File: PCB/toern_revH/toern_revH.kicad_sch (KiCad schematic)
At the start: 123 parts, among them IC1 BQ24075TRGTR, J1 AudioJack3_Switch, J10 Conn_01x02, J11 Conn_01x05, J11.5 Conn_01x05, J12 Conn_01x05, J13 Conn_01x05, J14 Conn_01x05, J15 Conn_01x05, J16 Conn_01x02, J17 AudioJack3_Ground, J18 Conn_01x05_Socket, J19 Conn_01x05_Socket, J2 Conn_01x05_Socket, J20 Conn_01x05_Socket, J21 Conn_01x05_Socket, J22 Conn_01x05_Socket, J23 Conn_01x05_Socket, J24 Conn_01x05_Socket, J25 Conn_01x02, J26 Conn_01x02, J3 AudioJack3_Ground, J4 USB_C_Receptacle_USB2.0, J5 AudioJack3_Switch, J6 AudioJack3_Switch, J7 AudioJack3_Switch, J8 Micro_SD_Card, J9 Conn_01x03, U1 SPX3819M5-L-3-3, U10 01x05 Connector_PinSocket_2.5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, U11 01x05 Connector_PinSocket_2.5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, U12 01x05 Connector_PinSocket_2.5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, U13 PAM8403D, U14 74LVC1G17, U15 74AHCT1G125, U2 SPX3819M5-L-1-8, U3 SGTL5000XNBA3, U4 TLP2361V4_E, U5 74LVC2G14, U6 Teensy4.1, U7 SPX3819M5-L-3-3, U8 TPS22918DBVR, U9 01x05 Connector_PinSocket_2.5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

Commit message: fixed production files for revH
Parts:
- removed TP1, TP2: TestPoint, symbol Connector:TestPoint
- C32: value 10uF -> 10u
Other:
- moved on the sheet: C21, C22, C38, J26, J8, R16, R29, R30, U14

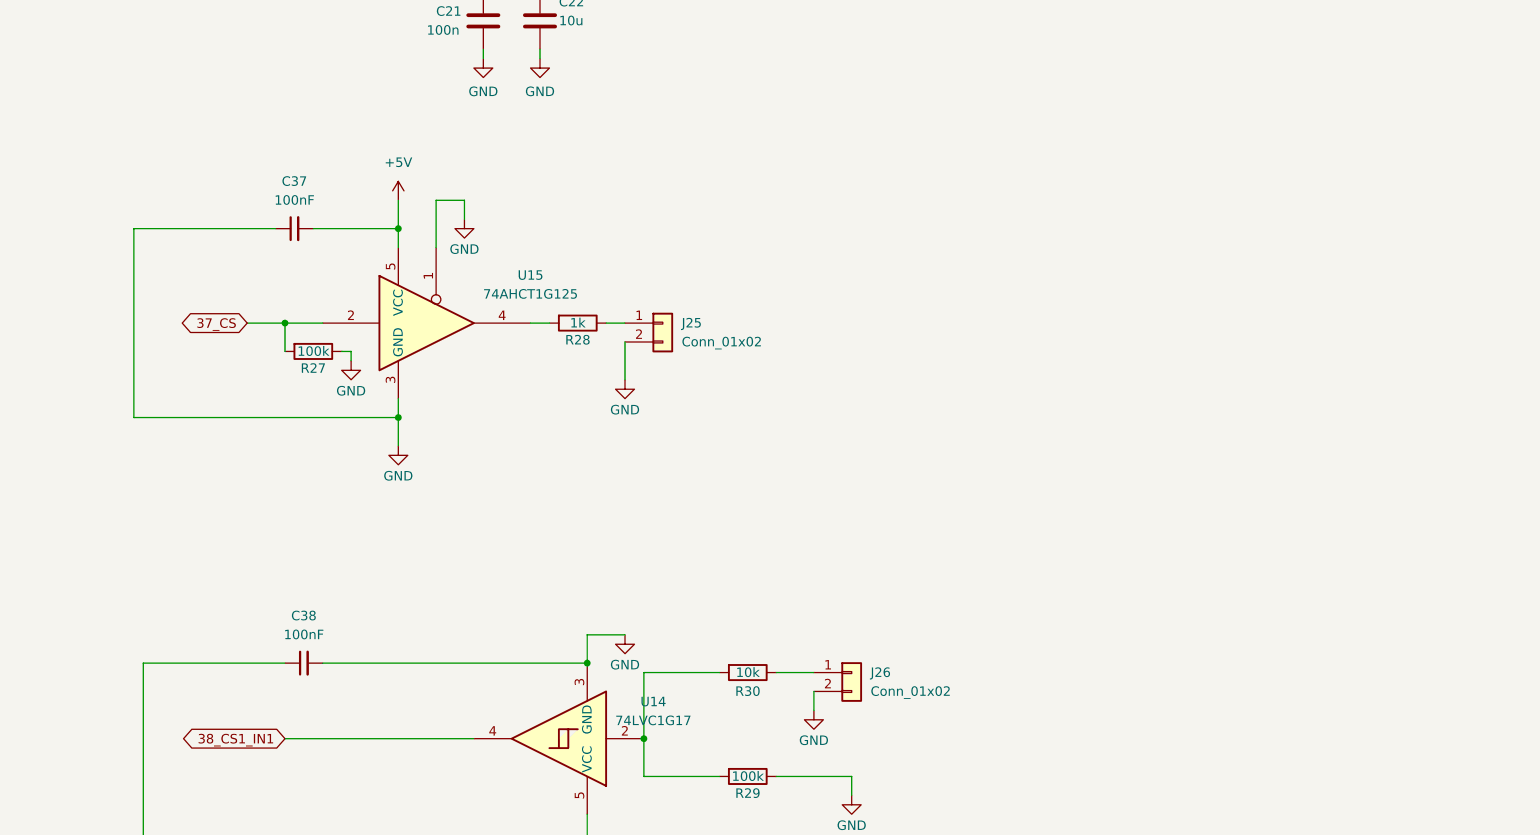
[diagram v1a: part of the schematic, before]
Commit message: added protection for 5-12v clock input as well as 2nd clockout
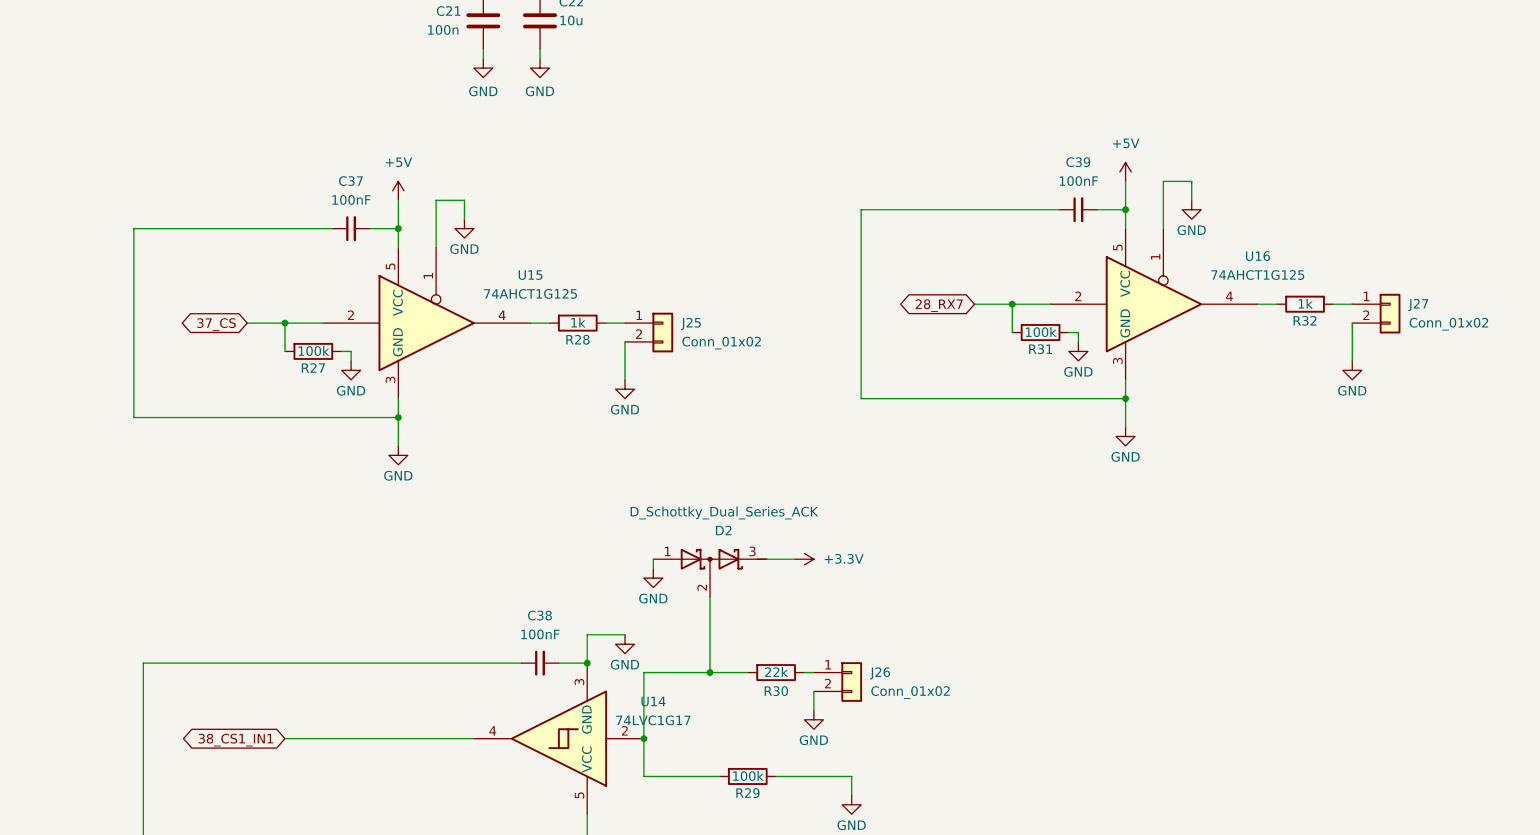
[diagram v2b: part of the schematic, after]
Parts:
- added C39: 100nF, Capacitor_SMD:C_0402_1005Metric, symbol Device:C_Small
- added D2: D_Schottky_Dual_Series_ACK, Package_TO_SOT_SMD:SOT-23, symbol Device:D_Schottky_Dual_Series_ACK
- added J27: Conn_01x02, Connector_JST:JST_PH_B2B-PH-K_1x02_P2.00mm_Vertical, symbol Connector_Generic:Conn_01x02
- added R31: 100k, Resistor_SMD:R_0402_1005Metric, symbol Device:R
- added R32: 1k, Resistor_SMD:R_0402_1005Metric, symbol Device:R
- added U16: 74AHCT1G125, Package_TO_SOT_SMD:SOT-23-5, symbol 74xGxx:74AHCT1G125
- R30: value 10k -> 22k; lcsc# C25744 -> C25768
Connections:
- net +3.3V: now also D2.3 (K)
- net +5V: now also C39.2, U16.5 (VCC)
- net 28_RX7: now also R31.2, U16.2
- net GND: now also C39.1, D2.1 (A), J27.2 (Pin_2), R31.1, U16.1, U16.3 (GND)
- net at R29.2, R30.2, U14.2: now also D2.2 (common)
- new net: J27.1 (Pin_1), R32.1
- new net: R32.2, U16.4
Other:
- moved on the sheet: C37, C38, R30

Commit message: added pogo pins and connectors to pcv revH
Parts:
- removed R11: 2.2k, Resistor_SMD:R_0603_1608Metric, symbol Device:R
- added CN1, CN2: YZP0354-20100-01, YZP0354-20100-01:YZP0354-20100-01, symbol YZP0354-20100-01:YZP0354-20100-01
- added MountingHole3: MountingHole_2.2mm_M2, MountingHole:MountingHole_2.2mm_M2, symbol Mechanical:MountingHole
- MK1: footprint Sensor_Audio:POM-2244P-C3310-2-R -> C529951:MIC-TH_BD6.0-P1.90-D0.4-L-FD
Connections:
- net D+: now also CN2.1 (CONTACT)
- net D-: now also CN1.1 (CONTACT)
- net GND: now also MK1.2 (-); no longer MK1.1 (-)
- net MICBIAS: now also J7.TN, MK1.1 (+)
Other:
- moved on the sheet: C20, J7, MK1, R27, R31

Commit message: updated BAT45s Pins on PCB+Shematics
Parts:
- D2: value D_Schottky_Dual_Series_ACK -> BAT54S; symbol Device:D_Schottky_Dual_Series_ACK -> toern:BAT54S
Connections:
- net +3.3V: now also D2.2 (K); no longer D2.3 (K)
- net at R29.2, R30.2, U14.2: now also D2.3 (common); no longer D2.2 (common)
